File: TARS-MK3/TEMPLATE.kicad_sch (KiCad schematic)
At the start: 4 parts, among them J1 Conn_02x12_Odd_Even, J2 Conn_02x12_Odd_Even, J3 Conn_02x12_Odd_Even, J4 Conn_02x12_Odd_Even

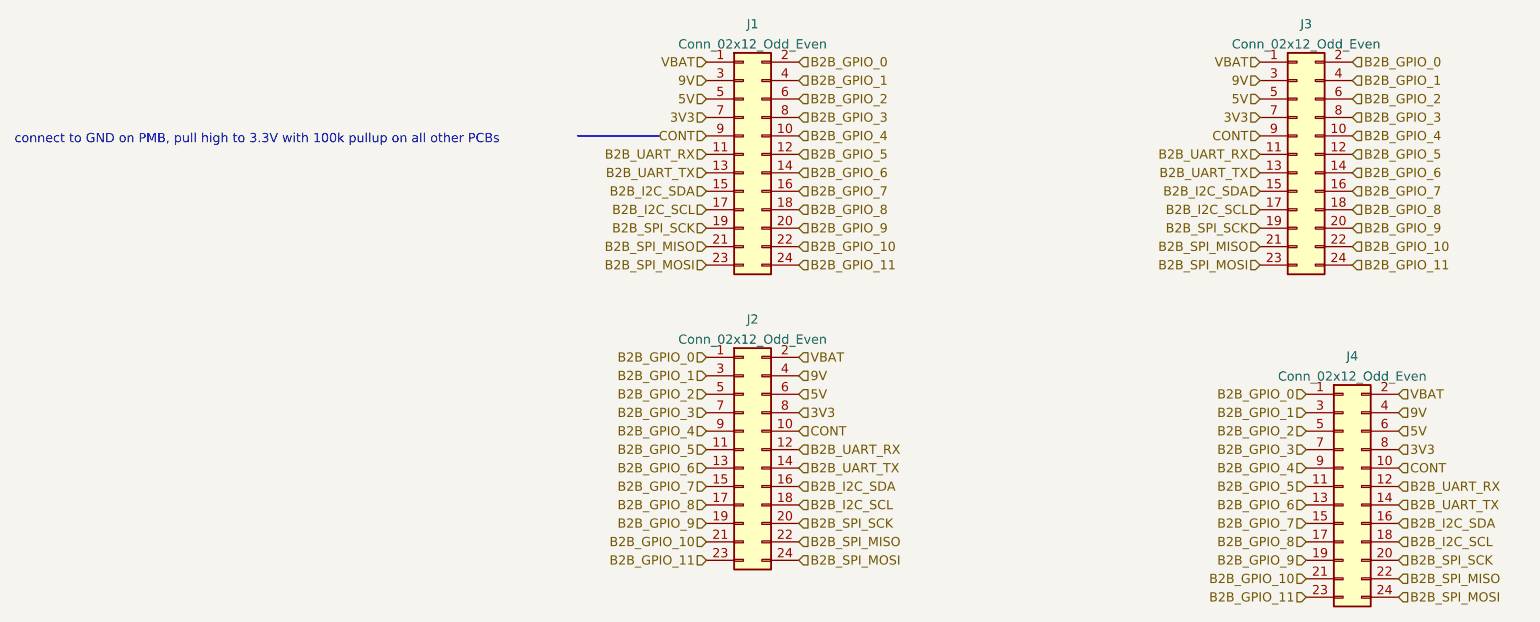
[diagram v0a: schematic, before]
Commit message: Routed B2Bs
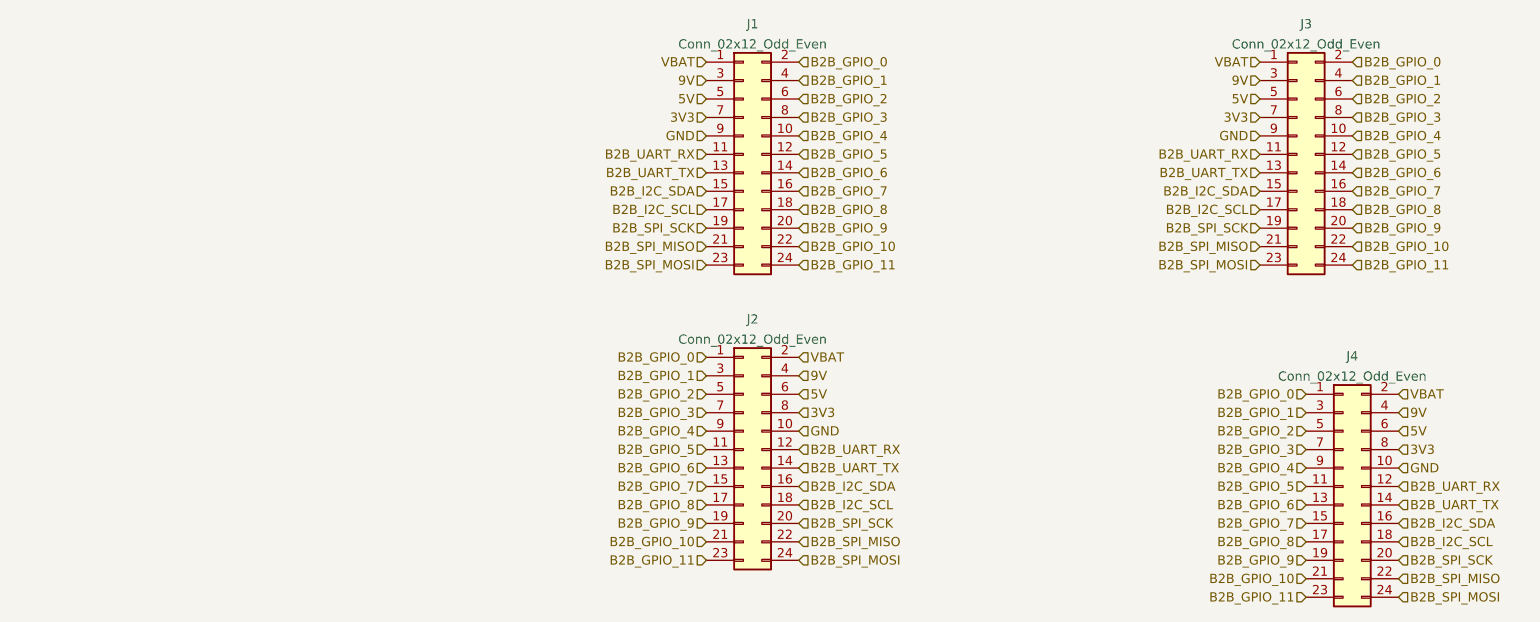
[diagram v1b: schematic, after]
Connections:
- net CONT renamed GND
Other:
- note removed: "connect to GND on PMB, pull high to 3.3V with 100k pullup on all other PCBs"
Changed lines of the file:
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@@
 (kicad_sch (version 20211123) (generator eeschema)
   (paper "A4")
-  (polyline (pts (xy 22.86 68.58) (xy 34.29 68.58))
-    (stroke (width 0) (type default) (color 0 0 0 0))
-  )
-  (text "connect to GND on PMB, pull high to 3.3V with 100k pullup on all other PCBs"
-    (at -54.61 69.85 0)
-    (effects (font (size 1.27 1.27)) (justify left bottom))
-  )
   (hierarchical_label "B2B_GPIO_4" (shape input) (at 53.34 68.58 0)
     (effects (font (size 1.27 1.27)) (justify left))
@@
     (effects (font (size 1.27 1.27)) (justify left))
   )
-  (hierarchical_label "CONT" (shape input) (at 135.89 114.3 0)
+  (hierarchical_label "GND" (shape input) (at 135.89 114.3 0)
     (effects (font (size 1.27 1.27)) (justify left))
   )
@@
     (effects (font (size 1.27 1.27)) (justify left))
   )
-  (hierarchical_label "CONT" (shape input) (at 116.84 68.58 180)
+  (hierarchical_label "GND" (shape input) (at 116.84 68.58 180)
     (effects (font (size 1.27 1.27)) (justify right))
   )
@@
     (effects (font (size 1.27 1.27)) (justify right))
   )
-  (hierarchical_label "CONT" (shape input) (at 53.34 109.22 0)
+  (hierarchical_label "GND" (shape input) (at 53.34 109.22 0)
     (effects (font (size 1.27 1.27)) (justify left))
   )
@@
     (effects (font (size 1.27 1.27)) (justify right))
   )
-  (hierarchical_label "CONT" (shape input) (at 40.64 68.58 180)
-    (effects (font (size 1.27 1.27)) (justify right))
-  )
+  (hierarchical_label "GND" (shape input) (at 40.64 68.58 180)
+    (effects (font (size 1.27 1.27)) (justify right))
+  )
